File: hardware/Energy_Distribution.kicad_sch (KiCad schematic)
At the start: 22 parts, among them J15 53398-0271, J16 53398-0671, J17 53398-0671, J18 53398-0271, U17 NVTFS5116PLTAG, U18 NVTFS5116PLTAG, U19 INA199C3DCKR, U21 LMV321RIYLT, U39 NVTFS5116PLTAG, U40 NVTFS5116PLTAG

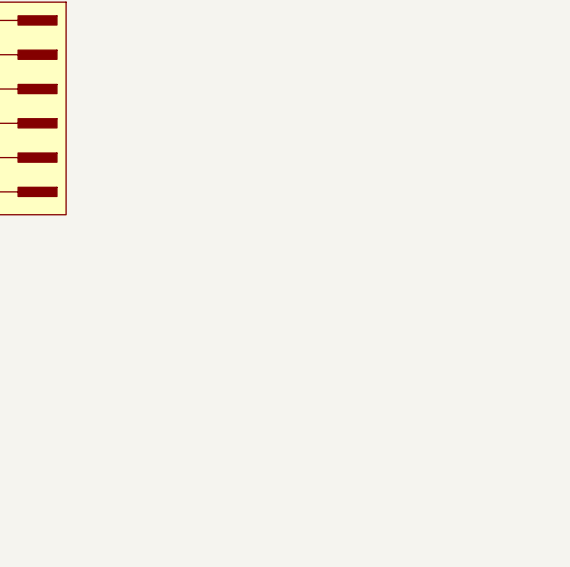
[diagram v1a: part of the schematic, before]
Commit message: hardware: Updating the custom design rules and library.
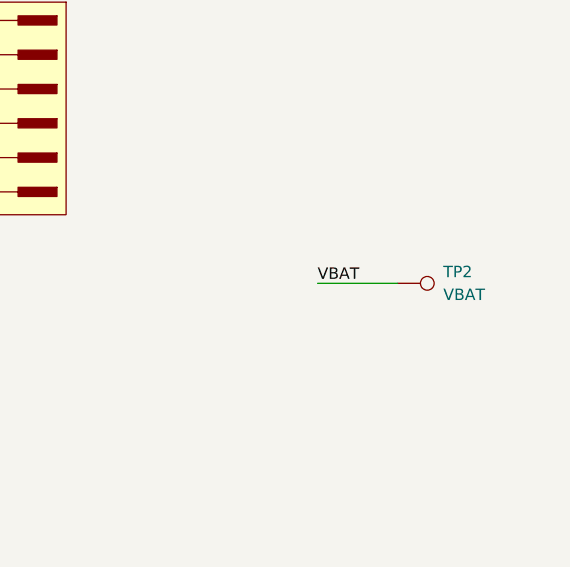
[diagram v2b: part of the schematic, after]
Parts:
- added TP2: VBAT, TestPoint:TestPoint_Pad_D1.0mm, symbol TESTPOINT:TestPoint
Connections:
- net VBAT: now also TP2.1
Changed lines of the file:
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@@
     (stroke (width 0) (type default))
+  )
+  (wire (pts (xy 256.54 140.97) (xy 265.43 140.97))
+    (stroke (width 0.5) (type default))
   )
   (wire (pts (xy 74.93 58.42) (xy 74.93 60.96))
@@
   (label "AMUX4" (at 241.3 27.94 0) (fields_autoplaced)
     (effects (font (size 0.8 0.8)) (justify left bottom))
+  )
+  (label "VBAT" (at 256.54 140.97 0) (fields_autoplaced)
+    (effects (font (size 1.27 1.27)) (justify left bottom))
   )
   (label "VBAT" (at 261.8592 44.45 0) (fields_autoplaced)
@@
         )
       )
+    )
+  )
+  (symbol (lib_id "TESTPOINT:TestPoint") (at 265.43 140.97 270) (unit 1)
+    (in_bom yes) (on_board yes) (dnp no) (fields_autoplaced)
+    (property "Reference" "TP2" (at 270.51 139.7 90)
+      (effects (font (size 1.27 1.27)) (justify left))
+    )
+    (property "Value" "VBAT" (at 270.51 142.24 90)
+      (effects (font (size 1.27 1.27)) (justify left))
+    )
+    (property "Footprint" "TestPoint:TestPoint_Pad_D1.0mm" (at 265.43 146.05 0)
+      (effects (font (size 1.27 1.27)) hide)
+    )
+    (property "Datasheet" "~" (at 265.43 146.05 0)
+      (effects (font (size 1.27 1.27)) hide)
+    )
+    (pin "1")
+    (instances
+      (project "eps-re_project"
+        (path "/2eebaa11-d7ed-4bfd-bc8e-988f68654d29/6f34948c-43a8-4614-b8ed-90c5b6b9b243"
+          (reference "TP2") (unit 1)
+        )
+        (path "/2eebaa11-d7ed-4bfd-bc8e-988f68654d29"
+          (reference "TP6") (unit 1)
+        )
+        (path "/2eebaa11-d7ed-4bfd-bc8e-988f68654d29/fd86ef80-5a59-4dab-8bcd-7bed00669ccc"
+          (reference "TP6") (unit 1)
+        )
+      )

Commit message: hardware: Adding blocking diodes. Pass through diodes were also added in MPPT-based converters. Also, test points were added.
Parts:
- TP2: footprint TestPoint:TestPoint_Pad_D1.0mm -> footprints:testpoint_smd
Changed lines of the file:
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@@
       (effects (font (size 1.27 1.27)) (justify left))
     )
-    (property "Footprint" "TestPoint:TestPoint_Pad_D1.0mm" (at 265.43 146.05 0)
+    (property "Footprint" "footprints:testpoint_smd" (at 265.43 146.05 0)
       (effects (font (size 1.27 1.27)) hide)
     )
